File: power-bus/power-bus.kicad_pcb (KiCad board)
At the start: 2 copper layers, 113.2 x 68.7 mm, 22 parts, among them J1 CONN_01X02, J10 CONN_01X02, J11 CONN_01X02, J2 CONN_01X02, J3 CONN_01X02, J4 CONN_01X02, J5 CONN_01X02, J6 CONN_01X02, J7 CONN_01X02, J8 CONN_01X02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

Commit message: Add more Vraw connectors to the power bus board.
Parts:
- removed J2, J3, J7: CONN_01X02, Connectors_Terminal_Blocks:TerminalBlock_Pheonix_MKDS1.5-2pol
- removed U1: pololu-vreg, conservify:pololu-vreg
- removed U2: pololu-vreg, conservify:pololu-vreg-adjustable
- added J12: CONN_01X02, conservify:TerminalBlock_Phoenix_MKDS1.5-2pol, F.Cu at (190.7, 109.8)
- added J13: CONN_01X02, conservify:TerminalBlock_Phoenix_MKDS1.5-2pol, F.Cu at (168.0, 112.9)
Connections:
- J9 pad 1: /12V0_3_EN -> Net-(J9-Pad1)
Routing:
- net /12V0_3_EN: track 71.2 -> 0.00 mm
- net /5V0_1: track 26.8 -> 0.00 mm
- net /VRAW: track 6.81 -> 21.0 mm
- removed copper zone on B.Cu, net /12V0_3
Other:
- board text added: "Vin"
- board text added: "v0.2"
- board text removed: "12V-1"
- board text removed: "12V1-EN"
- board text removed: "5V-1"
- board text removed: "v0.1"

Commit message: Fix library references, using our lib.
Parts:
- F1: footprint conservify:Fuseholder6x30_horiz_open_inline_Type-I -> conservify:FUSE_HOLDER_6x30
- J1, J10, J11, J4, J5, J6, J8: footprint Connectors_Terminal_Blocks:TerminalBlock_Pheonix_MKDS1.5-2pol -> conservify:TERMINAL_BLOCK_PHOENIX_MKDS1.5-2pol
- J12, J13: footprint conservify:TerminalBlock_Phoenix_MKDS1.5-2pol -> conservify:TERMINAL_BLOCK_PHOENIX_MKDS1.5-2pol
- J9: footprint Socket_Strips:Socket_Strip_Straight_1x05_Pitch2.54mm -> conservify:Socket_Strip_Straight_1x05_Pitch2.54mm
- U3, U4: footprint conservify:pololu-vreg-adjustable -> conservify:POLOLU_VREG_ADJUSTABLE

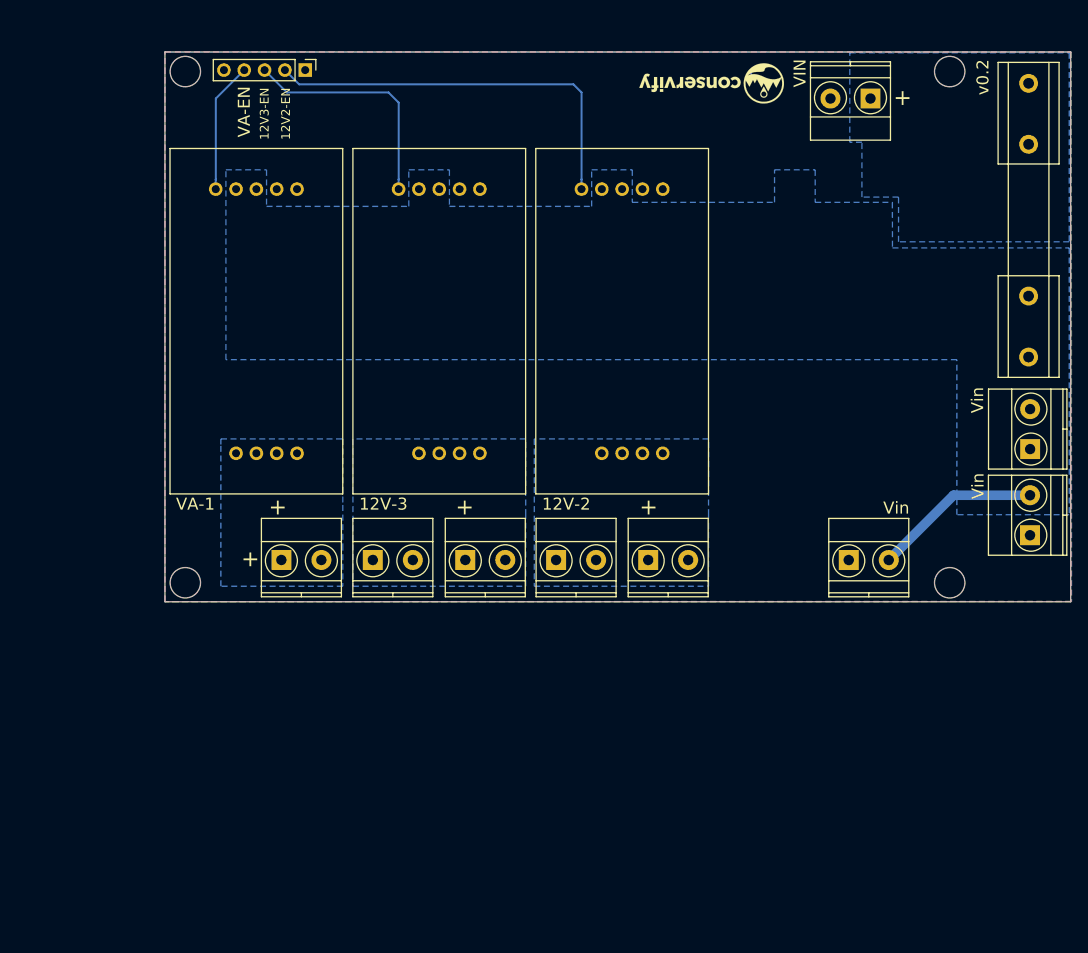
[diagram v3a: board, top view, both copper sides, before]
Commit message: New board design with several new features.
Relays build into board. RTC for the Pi. MCU and RockBlock connector.
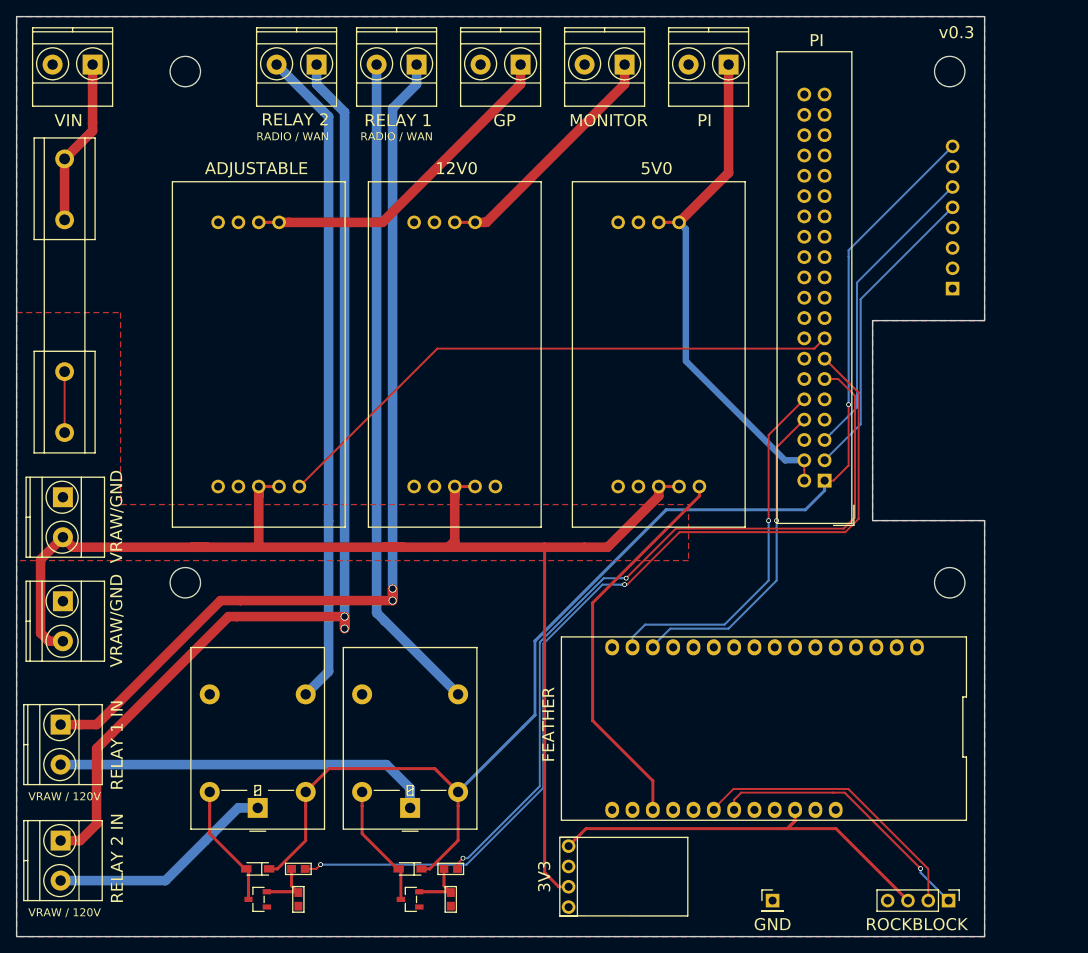
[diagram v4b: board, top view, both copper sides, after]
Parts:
- removed G***: LOGO, conservify:conservify_text_negative_4000
- added D1: 1N4148, conservify:SOD-123, F.Cu at (113.2, 151.5)
- added D2: 1N4148, conservify:SOD-123, F.Cu at (94.1, 151.5)
- added J14: CONN_01x01, conservify:Socket_Strip_Straight_1x01_Pitch2.54mm, F.Cu at (158.5, 155.5)
- added J2: CONN_GP, conservify:TERMINAL_BLOCK_PHOENIX_MKDS1.5-2pol, F.Cu at (127.0, 51.0)
- added J3: RPI, conservify:IDC-Header_2x20_P2.54mm_Vertical, F.Cu at (165.0, 103.0)
- added J7: CONN_RB, conservify:Socket_Strip_Straight_1x04_Pitch2.54mm, F.Cu at (180.5, 155.5)
- added K1: G5LE-1, conservify:Relay_SPDT_Omron-G5LE-1, F.Cu at (113.2, 143.9)
- added K2: G5LE-1, conservify:Relay_SPDT_Omron-G5LE-1, F.Cu at (94.1, 143.9)
- added Q1: MMBT2222, conservify:SOT-23, F.Cu at (113.2, 155.3)
- added Q2: MMBT2222, conservify:SOT-23, F.Cu at (94.1, 155.3)
- added R1: 1K, conservify:RES-0603, F.Cu at (118.3, 151.5)
- added R2: 1K, conservify:RES-0603, F.Cu at (118.3, 155.3)
- added R3: 1K, conservify:RES-0603, F.Cu at (99.2, 151.5)
- added R4: 1K, conservify:RES-0603, F.Cu at (99.2, 155.3)
- added U1: VREG_GP, conservify:POLOLU_VREG_ADJUSTABLE, F.Cu at (93.0, 88.5)
- added U2: ADAFRUIT_FEATHER, conservify:ADAFRUIT_FEATHER, F.Cu at (157.5, 134.0)
- J1: value CONN_01X02 -> CONN_VIN
- J10: value CONN_01X02 -> CONN_V_RAW
- J11: value CONN_01X02 -> CONN_V_RELAY_1
- J12, J13: value CONN_01X02 -> CONN_V_RELAY_2
- J4: value CONN_01X02 -> CONN_MON
- J5: value CONN_01X02 -> CONN_PI
- J6: value CONN_01X02 -> DS3231; footprint conservify:TERMINAL_BLOCK_PHOENIX_MKDS1.5-2pol -> conservify:Socket_Strip_Straight_1x08_Pitch2.54mm; moved to B.Cu
- J8: value CONN_01X02 -> CONN_GND
- J9: value CONN_01X05 -> CONN_V_RELAY_1; footprint conservify:Socket_Strip_Straight_1x05_Pitch2.54mm -> conservify:TERMINAL_BLOCK_PHOENIX_MKDS1.5-2pol
- U3: value pololu-vreg -> VREG_MON
- U4: value pololu-vreg -> VREG_PI
- U5: value pololu-vreg -> VREG_MCU; footprint conservify:pololu-vreg-adjustable -> conservify:POLOLU_VREG
- moved J12 127.0 mm to (69.5, 148.0), turned to 270 degrees
- moved J8 122.4 mm to (69.8, 118.1), turned to 270 degrees
- moved F1 120.9 mm to (70.0, 97.0)
- moved J1 97.3 mm to (73.5, 51.0)
- moved J13 90.9 mm to (101.5, 51.0), turned to 180 degrees
- moved J6 90.5 mm to (181.0, 79.0)
- moved U5 80.1 mm to (133.0, 152.5), turned to 270 degrees
- moved J5 70.1 mm to (153.0, 51.0), turned to 180 degrees
- moved J10 62.1 mm to (69.8, 105.1), turned to 270 degrees
- moved J4 62.0 mm to (140.0, 51.0), turned to 180 degrees
- moved J11 44.1 mm to (69.5, 133.5), turned to 270 degrees
- moved U4 25.8 mm to (143.0, 88.5), turned to 270 degrees
- moved U3 24.4 mm to (117.5, 88.5), turned to 270 degrees
- moved J9 13.9 mm to (114.0, 51.0), turned to 180 degrees
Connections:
- J10 pad 1: /12V0_1 -> GND
- J10 pad 2: GND -> /VRAW
- J11 pad 1: /12V0_2 -> /V_RELAY_1_GND
- J11 pad 2: GND -> /V_RELAY_1_IN
- J12 pad 1: GND -> /V_RELAY_2_GND
- J12 pad 2: /VRAW -> /V_RELAY_2_IN
- J13 pad 1: GND -> /V_RELAY_2_GND
- J13 pad 2: /VRAW -> /V_RELAY_2
- J4 pad 1: /12V0_1 -> /V_MON
- J5 pad 1: /12V0_2 -> /PI_5V0
- J6 pad 1: /VADJ_1 -> Net-(J6-Pad1)
- J6 pad 2: GND -> Net-(J6-Pad2)
- J9 pad 1: Net-(J9-Pad1) -> /V_RELAY_1_GND
- J9 pad 2: /12V0_1_EN -> /V_RELAY_1
- U3 pad 1: /12V0_1 -> /V_MON
- U3 pad 4: /12V0_1_EN -> Net-(U3-Pad4)
- U4 pad 1: /12V0_2 -> /PI_5V0
- U4 pad 4: /12V0_2_EN -> /V_PI_EN
- U5 pad 1: /VADJ_1 -> /V_MCU
- U5 pad 4: /VADJ_1_EN -> Net-(U5-Pad4)
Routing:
- net /PI_3V3: track 0.00 -> 162.8 mm, vias 0 -> 1
- net /VRAW: track 21.0 -> 177.4 mm
- net /V_RELAY_2_GND: track 0.00 -> 126.1 mm, vias 0 -> 2
- net /V_RELAY_2_EN: track 0.00 -> 119.6 mm, vias 0 -> 2
- net /V_RELAY_1_GND: track 0.00 -> 117.7 mm, vias 0 -> 2
- net /V_RELAY_1_EN: track 0.00 -> 98.7 mm, vias 0 -> 2
- net /V_RELAY_1: track 0.00 -> 82.9 mm
- net /V_RELAY_2: track 0.00 -> 82.6 mm
- net /V_GP_EN: track 0.00 -> 73.3 mm
- net /PI_5V0: track 0.00 -> 65.0 mm
- net /V_MCU: track 0.00 -> 52.9 mm
- net /12V0_1_EN: track 50.3 -> 0.00 mm
- net /V_PI_EN: track 0.00 -> 49.1 mm
- net /V_RELAY_1_IN: track 0.00 -> 47.4 mm
- net /PI_RX: track 0.00 -> 45.7 mm, vias 0 -> 1
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- added copper zone on F.Cu, net /VRAW
- removed copper zone on B.Cu, net /12V0_1
- removed copper zone on B.Cu, net /12V0_2
- removed copper zone on B.Cu, net /VADJ_1
- removed copper zone on B.Cu, net /VIN
- removed copper zone on B.Cu, net /VRAW
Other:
- board size 113.2 x 68.7 mm -> 121 x 115 mm
- board text added: "12V0"
- board text added: "3V3"
- board text added: "5V0"
- board text added: "ADJUSTABLE"
- board text added: "DS3231"
- board text added: "FEATHER"
- board text added: "GND"
- board text added: "GP"
- board text added: "MONITOR"
- board text added: "PI"
- board text added: "RADIO / WAN"
- board text added: "RELAY 1"
- board text added: "RELAY 1 IN"
- board text added: "RELAY 2"
- board text added: "RELAY 2 IN"
- board text added: "ROCKBLOCK"
- board text added: "VRAW / 120V"
- board text added: "VRAW/GND"
- board text added: "v0.3"
- board text removed: "+"
- board text removed: "12V-2"
- board text removed: "12V-3"
- board text removed: "12V2-EN"
- board text removed: "12V3-EN"
- board text removed: "VA-1"
- board text removed: "VA-EN"
- board text removed: "Vin"
- board text removed: "v0.2"
